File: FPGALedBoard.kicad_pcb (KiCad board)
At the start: 2 copper layers, 59 parts, among them J1 Conn_02x20_Odd_Even, U1 74AHC04, U2 74AHC04, U3 74AHC04, U4 74AHC04, U5 74AHC04, U6 D148K, U7 74AHC04, U8 D148K

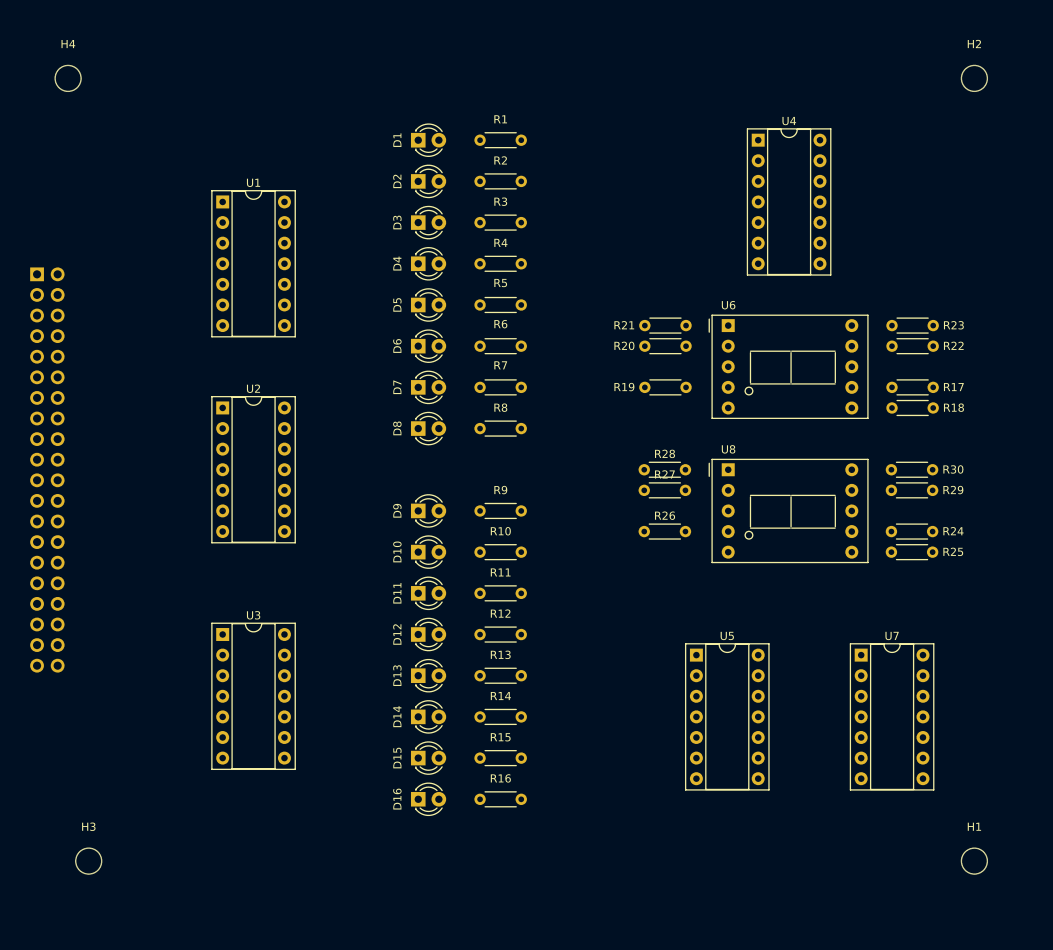
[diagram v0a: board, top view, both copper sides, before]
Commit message: Atualizados os Footprints. Definido um primeiro corte da placa.
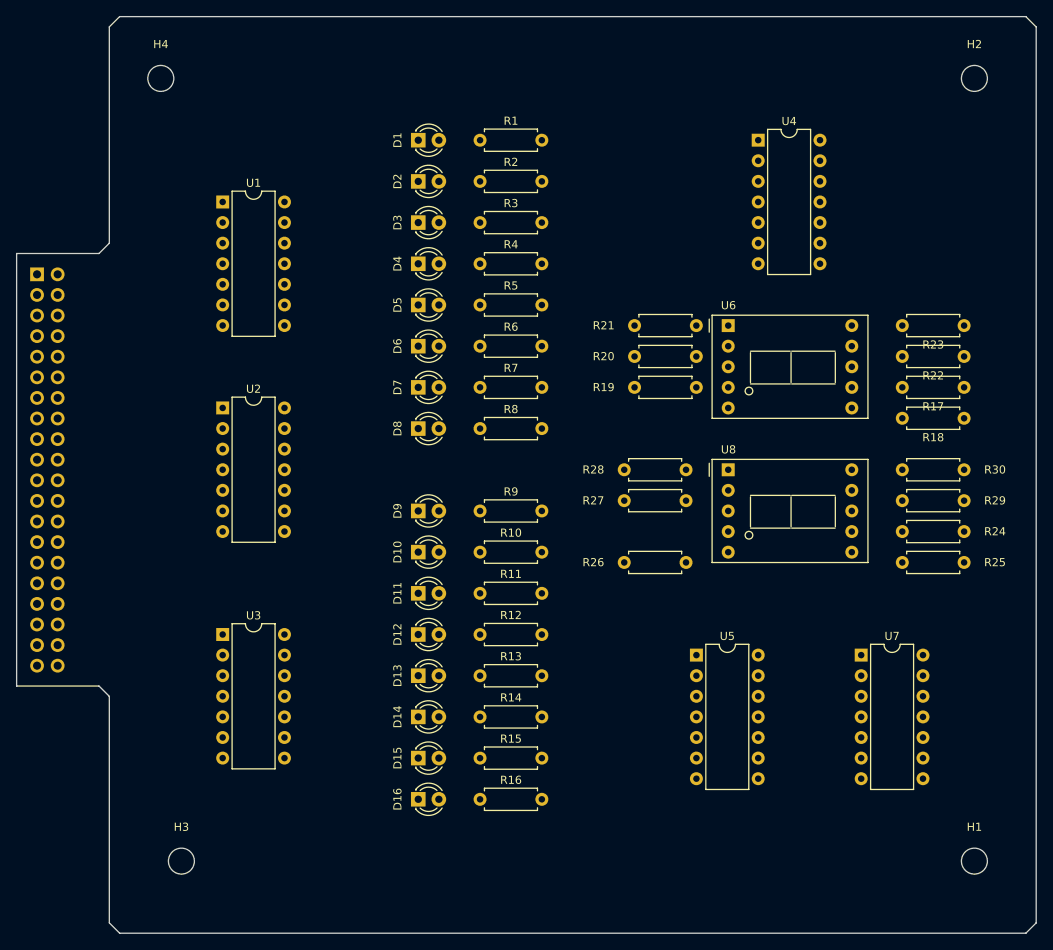
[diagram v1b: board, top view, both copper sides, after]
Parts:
- R1, R10, R11, R12, R13, R14, R15, R16, R17, R18, R19, R2, R20, R21, R22, R23, R24, R25, R26, R27, R28, R29, R3, R30, R4, R5, R6, R7, R8, R9: footprint Resistor_THT:R_Axial_DIN0204_L3.6mm_D1.6mm_P5.08mm_Horizontal -> Resistor_THT:R_Axial_DIN0207_L6.3mm_D2.5mm_P7.62mm_Horizontal
- U1, U2, U3, U4, U5, U7: footprint Package_DIP:DIP-14_W7.62mm_Socket -> Package_DIP:DIP-14_W7.62mm
- moved H4 11.4 mm to (97.8, 38.1)
- moved H3 11.4 mm to (100.3, 134.6)
- moved R26 4.54 mm to (154.9, 97.8)
- moved R25 4.08 mm to (196.8, 97.8)
- moved R29 4.08 mm to (196.8, 90.2)
- moved R18 4.02 mm to (196.8, 80.0)
- moved R22 4.02 mm to (196.8, 72.4)
- moved R30 3.88 mm to (196.8, 86.4)
- moved R17 3.81 mm to (196.8, 76.2)
- moved R23 3.81 mm to (196.8, 68.6)
- moved R27 2.78 mm to (154.9, 90.2)
- moved R28 2.47 mm to (154.9, 86.4)
- moved R20 1.80 mm to (156.2, 72.4)
- moved R24 1.34 mm to (189.2, 94.0)
- moved R19 1.27 mm to (156.2, 76.2)
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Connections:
- U1 pad 14: +3V3 -> +5V
- U2 pad 14: +3V3 -> +5V
- U3 pad 14: +3V3 -> +5V
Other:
- board outline added: 125.7 x 113 mm

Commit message: Placa roeada automaticamente.
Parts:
- removed U7: 74AHC04, Package_DIP:DIP-14_W7.62mm
- added C1: 10uF, Capacitor_THT:CP_Radial_D5.0mm_P2.50mm, F.Cu at (105.4, 45.7)
- added C2: 10uF, Capacitor_THT:CP_Radial_D5.0mm_P2.50mm, F.Cu at (105.4, 72.4)
- added C3: 10uF, Capacitor_THT:CP_Radial_D5.0mm_P2.50mm, F.Cu at (105.4, 100.3)
- added C4: 10uF, Capacitor_THT:CP_Radial_D5.0mm_P2.50mm, F.Cu at (158.8, 41.9)
- added C5: 10uF, Capacitor_THT:CP_Radial_D5.0mm_P2.50mm, F.Cu at (157.5, 105.4)
- moved R17 96.1 mm to (109.2, 115.6), turned to -90 degrees
- moved R18 91.1 mm to (113.0, 115.6), turned to -90 degrees
- moved R25 55.0 mm to (144.8, 115.6), turned to 90 degrees
- moved R24 54.0 mm to (162.6, 47.0), turned to -90 degrees
- moved R30 46.0 mm to (161.3, 115.6), turned to 90 degrees
- moved R29 40.7 mm to (165.1, 115.6), turned to 90 degrees
- moved R28 39.9 mm to (161.3, 125.7), turned to 90 degrees
- moved R27 37.0 mm to (144.8, 125.7), turned to 90 degrees
- moved R23 35.4 mm to (162.6, 59.7), turned to -90 degrees
- moved R22 33.0 mm to (166.4, 59.7), turned to -90 degrees
- moved R19 32.4 mm to (142.2, 47.0), turned to -90 degrees
- moved H1 31.4 mm to (167.6, 127.0)
- moved R26 31.2 mm to (141.0, 125.7), turned to 90 degrees
- moved H2 30.9 mm to (167.6, 43.2)
- moved U6 20.9 mm to (147.4, 73.7)
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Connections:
- U3 pad 10: (no net) -> Net-(R17-Pad1)
- U3 pad 11: (no net) -> /C1
- U3 pad 12: (no net) -> Net-(R18-Pad1)
- U3 pad 13: (no net) -> /C2
- U4 pad 10: Net-(R17-Pad1) -> Net-(R23-Pad1)
- U4 pad 11: /C1 -> /C7
- U4 pad 12: Net-(R18-Pad1) -> Net-(R24-Pad1)
- U4 pad 13: /C2 -> /D1
- U4 pad 14: (no net) -> +5V
- U4 pad 7: (no net) -> GND
- U5 pad 10: Net-(R23-Pad1) -> Net-(R29-Pad1)
- U5 pad 11: /C7 -> /D6
- U5 pad 12: Net-(R24-Pad1) -> Net-(R30-Pad1)
- U5 pad 13: /D1 -> /D7
- U5 pad 14: (no net) -> +5V
- U5 pad 7: (no net) -> GND
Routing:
- net GND: track 0.00 -> 307.6 mm
- net +5V: track 0.00 -> 267.1 mm
- net /C3: track 0.00 -> 101.4 mm
- net /D5: track 0.00 -> 95.0 mm
- net /D6: track 0.00 -> 94.4 mm
- net /D1: track 0.00 -> 93.3 mm
- net /C7: track 0.00 -> 84.2 mm
- net /C6: track 0.00 -> 83.7 mm, vias 0 -> 1
- net Net-(R17-Pad2): track 0.00 -> 77.8 mm
- net /D7: track 0.00 -> 77.7 mm
- net /D4: track 0.00 -> 77.4 mm, vias 0 -> 1
- net /D3: track 0.00 -> 76.4 mm, vias 0 -> 1
- net /D2: track 0.00 -> 76.3 mm, vias 0 -> 1
- net Net-(R18-Pad2): track 0.00 -> 75.0 mm
- net /C4: track 0.00 -> 73.4 mm
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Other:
- board size 125.7 x 113 mm -> 92.7 x 94 mm
- board text added: "IFTM - Campus Ituiutaba Ailton Siqueira Jr. Jan-2022 v1.0"

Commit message: Pequenas melhorias no Layout da placa
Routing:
- net Net-(D4-Pad1): track 19.4 -> 35.1 mm
- net /C3: track 101.4 -> 86.6 mm
- net GND: track 307.6 -> 310.0 mm
- net /D5: track 95.0 -> 96.2 mm
- net +5V: track 267.1 -> 268.1 mm
- net Net-(R28-Pad2): track 36.9 -> 36.2 mm

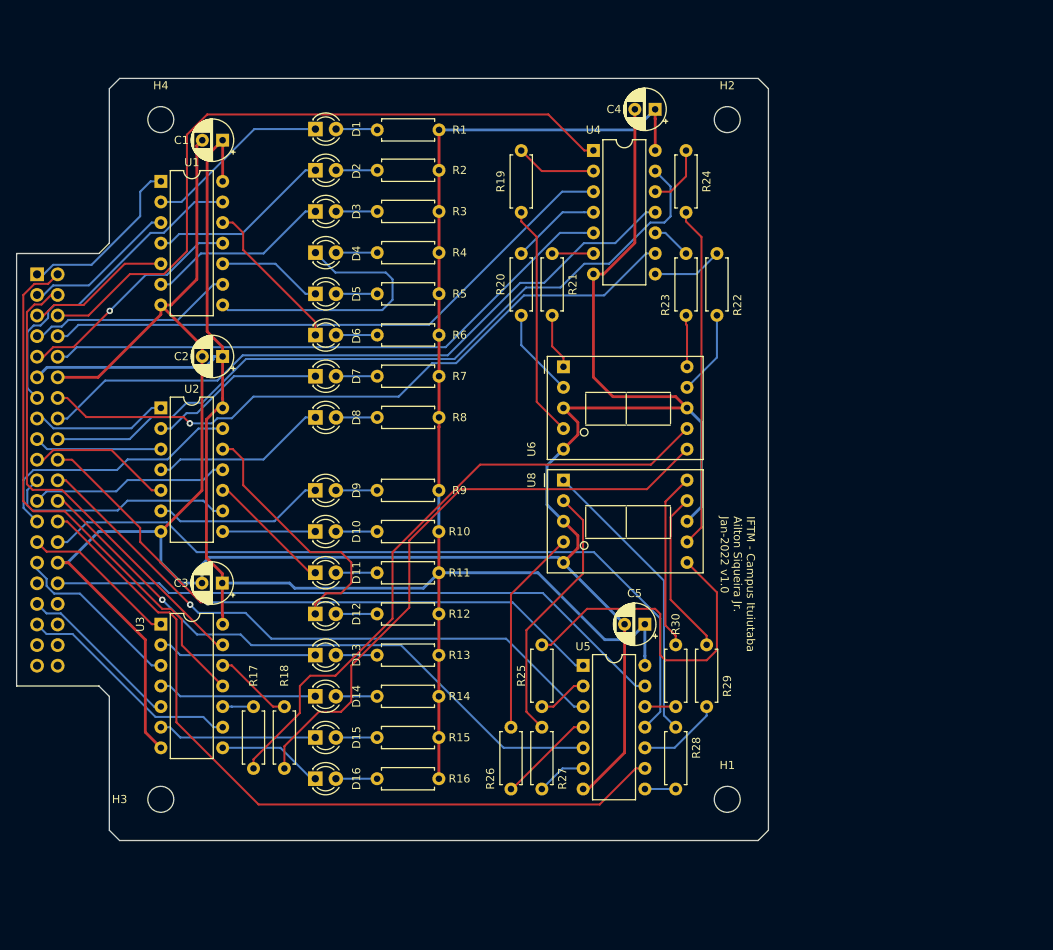
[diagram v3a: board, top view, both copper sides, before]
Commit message: Corrigido um erro na linha de 3.3V. Adicionado o Ground Plane.
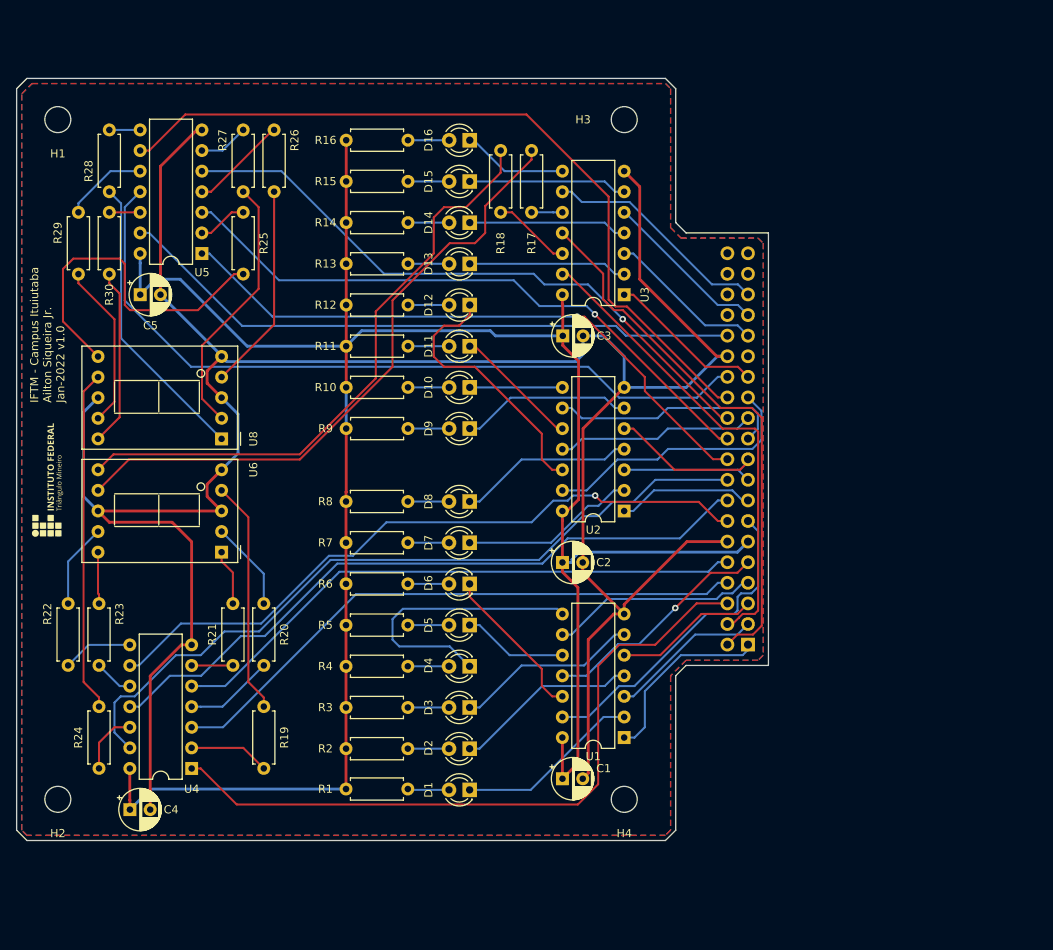
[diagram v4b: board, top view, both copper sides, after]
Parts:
- added G***: LOGO, Logo:IFTMLogoHor, F.Cu at (83.8, 87.6)
- moved H1 117.6 mm to (85.1, 43.2), turned to 180 degrees
- moved H2 117.6 mm to (85.1, 127.0), turned to 180 degrees
- moved C4 108.0 mm to (94.0, 128.3), turned to 0 degrees
- moved R28 107.2 mm to (91.4, 44.5), turned to -90 degrees
- moved R24 105.1 mm to (90.2, 123.2), turned to 90 degrees
- moved H3 101.4 mm to (154.9, 43.2), turned to 180 degrees
- moved H4 101.4 mm to (154.9, 127.0), turned to 180 degrees
- moved J1 98.8 mm to (170.2, 107.9), turned to 0 degrees
- moved R29 98.6 mm to (87.6, 54.6), turned to -90 degrees
- moved R22 94.8 mm to (86.4, 110.5), turned to 90 degrees
- moved R30 92.7 mm to (91.4, 54.6), turned to -90 degrees
- moved U4 90.9 mm to (101.6, 123.2), turned to 180 degrees
- moved U1 89.3 mm to (154.9, 119.4), turned to 180 degrees
- moved R27 89.2 mm to (108.0, 44.5), turned to -90 degrees
- moved C1 89.2 mm to (147.3, 124.5), turned to 0 degrees
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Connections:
- J1 pad 29: /LEDBAR_B6 -> +3V3
- J1 pad 31: +3V3 -> /LEDBAR_B6
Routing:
- net /LEDBAR_B6: track 21.5 -> 19.5 mm
- net /LEDBAR_A1: track 21.8 -> 23.0 mm
- net Net-(R25-Pad2): track 41.9 -> 42.8 mm
- net /LEDBAR_A6: track 39.8 -> 40.4 mm
- added copper zone on B.Cu, net GND
- added copper zone on F.Cu, net GND
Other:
- outline, holes or cut-outs redrawn
